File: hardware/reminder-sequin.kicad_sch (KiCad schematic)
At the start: 10 parts, among them SW1 User, SW2 RST, U1 STM32G041J6Mx

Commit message: power system
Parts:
- added BT1: Battery_Cell, Battery:BatteryHolder_Keystone_2466_1xAAA, symbol Device:Battery_Cell
- added C3, C4, C5: 10uF, Capacitor_SMD:C_0805_2012Metric, symbol Device:C
- added D2: SS24, Diode_SMD:D_SMA, symbol Device:D_Schottky
- added F1: Polyfuse, Fuse:Fuse_1206_3216Metric, symbol Device:Polyfuse
- added JP1: ISENSE, Jumper:SolderJumper-2_P1.3mm_Bridged2Bar_RoundedPad1.0x1.5mm, symbol Jumper:Jumper_2_Open
- added JP2: SolderJumper_2_Bridged, Jumper:SolderJumper-2_P1.3mm_Bridged2Bar_RoundedPad1.0x1.5mm, symbol Jumper:SolderJumper_2_Bridged
- added JP3: Power_Bypass, Jumper:SolderJumper-2_P1.3mm_Bridged2Bar_RoundedPad1.0x1.5mm, symbol Jumper:SolderJumper_2_Bridged
- added L1: 2.7uH, cat:Inductor_0806, symbol Device:L
- added R5: 487k, symbol Device:R
- added R6: 100k, symbol Device:R
- added U2: ~, symbol cat:TPS61023DRL
- D1, R1, R3: now not fitted
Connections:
- net GND: now also BT1.2 (-), C3.2, C4.2, C5.2, D2.2 (A), R6.2, U2.4 (GND)
- net VDD: now also JP3.2 (B)
- new net: C3.1, D2.1 (K), F1.2, JP2.1 (A), L1.1, U2.2 (EN), U2.3 (VIN)
- new net: C4.1, C5.1, JP3.1 (A), R5.1, U2.6 (VOUT)
- new net: R5.2, R6.1, U2.1 (FB)
- new net: L1.2, U2.5 (SW)
- new net: F1.1, JP1.2 (B)
- new net: BT1.1 (+), JP1.1 (A)
- new net BATTERY_SENSE: JP2.2 (B)

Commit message: stuff
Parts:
- removed U1: STM32G041J6Mx, Package_SO:SOIC-8_3.9x4.9mm_P1.27mm, symbol MCU_ST_STM32G0:STM32G041J6Mx
- added R7: 100k, symbol Device:R
- added U1: STM32G031F6Px, Package_SO:TSSOP-20_4.4x6.5mm_P0.65mm, symbol MCU_ST_STM32G0:STM32G031F6Px
- added U3: STM32G031J6Mx, Package_SO:SOIC-8_3.9x4.9mm_P1.27mm, symbol MCU_ST_STM32G0:STM32G031J6Mx
- D1: Cost (none) -> .5
- U2: value ~ -> TPS61023DRL; footprint (none) -> Package_TO_SOT_SMD:SOT-563; LCSC Part # (none) -> C919459
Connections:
- net BATTERY_SENSE: now also R7.1, U3.6 (PA10/PA12); no longer JP2.2 (B)
- net BUTTON: now also U3.8 (PA14/PA15/PB5/PB6)
- net GND: now also U1.5 (VSS), U3.3 (VSS)
- net LED: now also U3.1 (PB7/PB8/PB9/PC14)
- net NRST: now also U3.4 (PA0/PA1/PA2/PF2)
- net PHOTORESISTOR: now also U3.5 (PA8/PA9/PA11/PB0/PB1)
- net SWCK: now also U3.7 (PA13)
- net VDD: now also U1.4 (VDD), U3.2 (VDD)
- new net: JP2.2 (B), R7.2

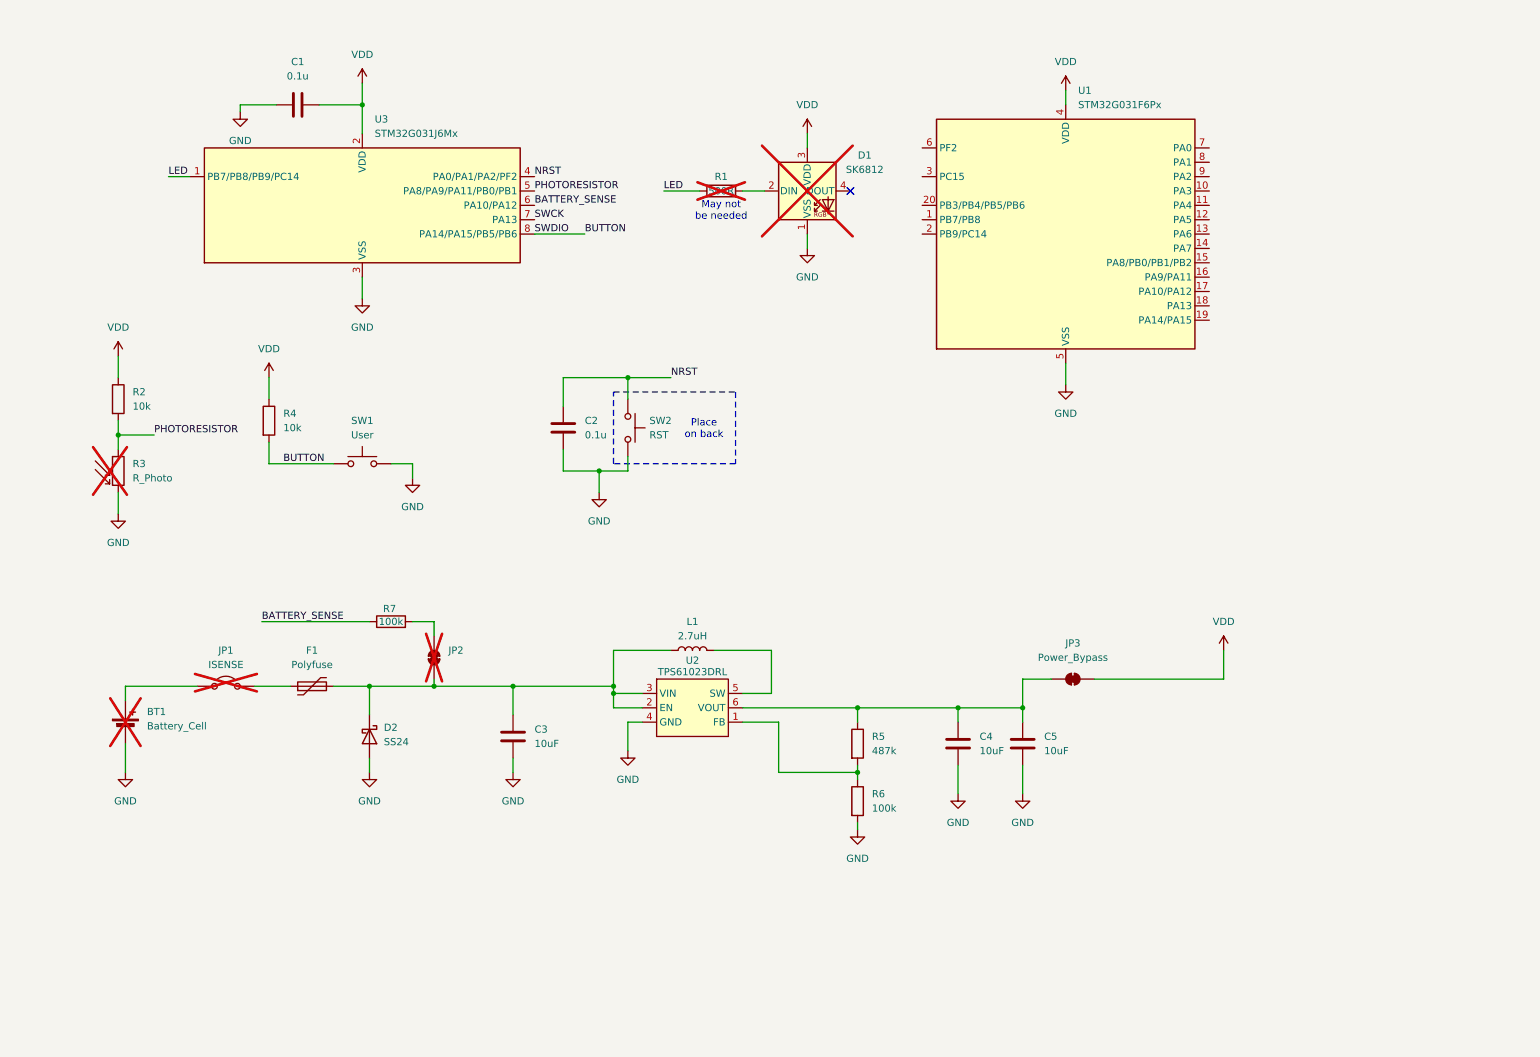
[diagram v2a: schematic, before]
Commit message: switched to rp2040
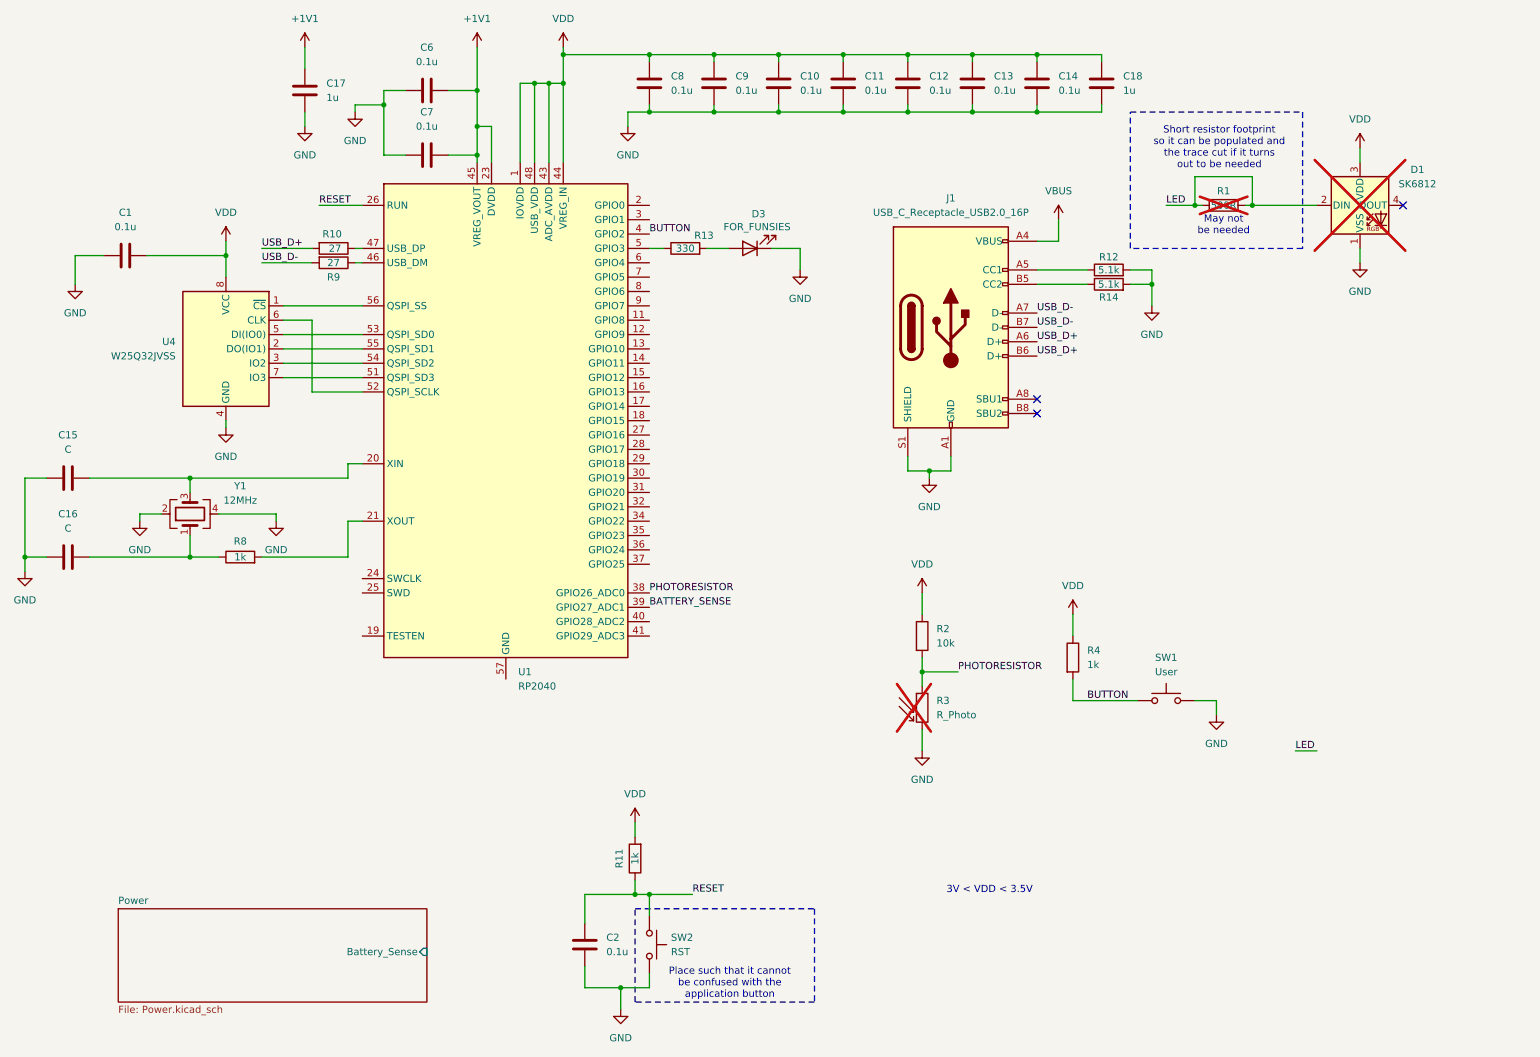
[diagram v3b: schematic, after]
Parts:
- removed BT1: Battery_Cell, Battery:BatteryHolder_Keystone_2466_1xAAA, symbol Device:Battery_Cell
- removed C3, C4, C5: 10uF, Capacitor_SMD:C_0805_2012Metric, symbol Device:C
- removed D2: SS24, Diode_SMD:D_SMA, symbol Device:D_Schottky
- removed F1: Polyfuse, Fuse:Fuse_1206_3216Metric, symbol Device:Polyfuse
- removed JP1: ISENSE, Jumper:SolderJumper-2_P1.3mm_Bridged2Bar_RoundedPad1.0x1.5mm, symbol Jumper:Jumper_2_Open
- removed JP2: SolderJumper_2_Bridged, Jumper:SolderJumper-2_P1.3mm_Bridged2Bar_RoundedPad1.0x1.5mm, symbol Jumper:SolderJumper_2_Bridged
- removed JP3: Power_Bypass, Jumper:SolderJumper-2_P1.3mm_Bridged2Bar_RoundedPad1.0x1.5mm, symbol Jumper:SolderJumper_2_Bridged
- removed L1: 2.7uH, cat:Inductor_0806, symbol Device:L
- removed R5: 487k, symbol Device:R
- removed R6, R7: 100k, symbol Device:R
- removed U1: STM32G031F6Px, Package_SO:TSSOP-20_4.4x6.5mm_P0.65mm, symbol MCU_ST_STM32G0:STM32G031F6Px
- removed U2: TPS61023DRL, Package_TO_SOT_SMD:SOT-563, symbol cat:TPS61023DRL
- removed U3: STM32G031J6Mx, Package_SO:SOIC-8_3.9x4.9mm_P1.27mm, symbol MCU_ST_STM32G0:STM32G031J6Mx
- added C10, C11, C12, C13, C14, C6, C7, C8, C9: 0.1u, Capacitor_SMD:C_0603_1608Metric, symbol Device:C
- added C15, C16: C, symbol Device:C
- added C17, C18: 1u, Capacitor_SMD:C_0805_2012Metric, symbol Device:C
- added D3: FOR_FUNSIES, symbol Device:LED
- added J1: USB_C_Receptacle_USB2.0_16P, Connector_USB:USB_C_Receptacle_G-Switch_GT-USB-7010ASV, symbol Connector:USB_C_Receptacle_USB2.0_16P
- added R10, R9: 27, Resistor_SMD:R_0603_1608Metric, symbol Device:R
- added R11, R8: 1k, Resistor_SMD:R_0603_1608Metric, symbol Device:R
- added R12, R14: 5.1k, Resistor_SMD:R_0603_1608Metric, symbol Device:R
- added R13: 330, Resistor_SMD:R_0603_1608Metric, symbol Device:R
- added U1: RP2040, Package_DFN_QFN:QFN-56-1EP_7x7mm_P0.4mm_EP3.2x3.2mm, symbol MCU_RaspberryPi:RP2040
- added U4: W25Q32JVSS, Package_SO:SOIC-8_5.23x5.23mm_P1.27mm, symbol Memory_Flash:W25Q32JVSS
- added Y1: 12MHz, symbol Device:Crystal_GND24
- C1, C2: footprint (none) -> Capacitor_SMD:C_0603_1608Metric; LCSC Part # (none) -> C14663
- R1: footprint (none) -> Resistor_SMD:R_0603_1608Metric
- R2: footprint (none) -> Resistor_SMD:R_0603_1608Metric; LCSC Part # (none) -> C25804
- R3: footprint (none) -> Connector_JST:JST_XH_B2B-XH-AM_1x02_P2.50mm_Vertical
- R4: value 10k -> 1k; footprint (none) -> Resistor_SMD:R_0603_1608Metric; LCSC Part # (none) -> C21190
- SW1, SW2: footprint (none) -> Button_Switch_SMD:SW_Push_1P1T_XKB_TS-1187A; LCSC Part # (none) -> C318884
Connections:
- net BATTERY_SENSE: now also U1.39 (GPIO27_ADC1)
- net BUTTON: now also U1.4 (GPIO2)
- net GND: now also C10.1, C11.1, C12.1, C13.1, C14.1, C15.1, C16.1, C17.1, C18.1, C6.1, C7.1, C8.1, C9.1, D3.1 (K), J1.A1 (GND), J1.A12 (GND), J1.B1 (GND), J1.B12 (GND), J1.S1 (SHIELD), R12.2, R14.2, U4.4 (GND), Y1.2, Y1.4
- net LED: now also D1.2 (DIN), R1.2
- net PHOTORESISTOR: now also U1.38 (GPIO26_ADC0)
- net VDD: now also C10.2, C11.2, C12.2, C13.2, C14.2, C18.2, C8.2, C9.2, R11.2, U1.1 (IOVDD), U1.10 (IOVDD), U1.22 (IOVDD), U1.33 (IOVDD), U1.42 (IOVDD), U1.43 (ADC_AVDD), U1.44 (VREG_IN), U1.48 (USB_VDD), U1.49 (IOVDD), U4.8 (VCC)
- net NRST renamed RESET
- net RESET: now also R11.1, U1.26 (RUN)
- new net: C15.2, U1.20 (XIN), Y1.3
- new net: C16.2, R8.1, Y1.1
- new net: R8.2, U1.21 (XOUT)
- new net: R13.1, U1.5 (GPIO3)
- new net: D3.2 (A), R13.2
- new net: J1.B5 (CC2), R14.1
- new net: U1.56 (QSPI_SS), U4.1 (~{CS})
- new net: U1.55 (QSPI_SD1), U4.2 (DO(IO1))
- new net: U1.54 (QSPI_SD2), U4.3 (IO2)
- new net: U1.53 (QSPI_SD0), U4.5 (DI(IO0))
- new net: U1.52 (QSPI_SCLK), U4.6 (CLK)
- new net: U1.51 (QSPI_SD3), U4.7 (IO3)
- new net: R9.1, U1.46 (USB_DM)
- new net: R10.1, U1.47 (USB_DP)
- new net: J1.A5 (CC1), R12.1
- new net +1V1: C17.2, C6.2, C7.2, U1.23 (DVDD), U1.45 (VREG_VOUT), U1.50 (DVDD)
- new net USB_D+: J1.A6 (D+), J1.B6 (D+), R10.2
- new net USB_D-: J1.A7 (D-), J1.B7 (D-), R9.2
- new net VBUS: J1.A4 (VBUS), J1.A9 (VBUS), J1.B4 (VBUS), J1.B9 (VBUS)
- no-connect marks 1 -> 3
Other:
- added sheet Power (Power.kicad_sch)
- note added: "3V < VDD < 3.5V"
- note added: "Place such that it cannot be confused with the application button"
- note added: "Short resistor footprint so it can be populated and the trace cut if it turns out to be needed"
- note removed: "Place on back"
- moved on the sheet: C2, D1, R1, R2, R3, R4, SW1, SW2

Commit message: almost done
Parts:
- added C19: 0.1u, Capacitor_SMD:C_0603_1608Metric, symbol Device:C
- added R15, R16, R17, R19, R20: 5.1k, Resistor_SMD:R_0603_1608Metric, symbol Device:R
- added R18, R22: 10k, Resistor_SMD:R_0603_1608Metric, symbol Device:R
- added R21: 1k, Resistor_SMD:R_0603_1608Metric, symbol Device:R
- added SW3: BOOTSEL, symbol Switch:SW_Push
- added TP1, TP2: TestPoint, symbol Connector:TestPoint
- added U3: FM24C64B, Package_SO:SOIC-8_3.9x4.9mm_P1.27mm, symbol Memory_NVRAM:FM24C64B
- SW1, SW2: footprint Button_Switch_SMD:SW_Push_1P1T_XKB_TS-1187A -> (none); LCSC Part # C318884 -> C720477
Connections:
- net BUTTON: now also U1.9 (GPIO7); no longer U1.4 (GPIO2)
- net GND: now also U1.19 (TESTEN), U1.57 (GND), C19.2, R15.1, R16.1, R17.1, SW3.2, U3.4 (VSS)
- net VDD: now also C19.1, R18.1, R19.2, R20.2, R22.1, U3.8 (VDD)
- net at R13.1: now also U1.11 (GPIO8); no longer U1.5 (GPIO3)
- net QSPI_CS: now reaches U1.56 (QSPI_SS), U4.1 (~{CS})
- net QSPI_CS: now also R21.1
- net at U1.2 (GPIO0): now also TP1.1
- net at U1.3 (GPIO1): now also TP2.1
- net EEPROM_WP: now reaches U1.6 (GPIO4)
- net EEPROM_WP: now also R18.2, U3.7 (WP)
- new net: R17.2, U3.1 (A0)
- new net: R16.2, U3.2 (A1)
- new net: R15.2, U3.3 (A2)
- new net: R21.2, R22.2, SW3.1
- new net SCL: R19.1, U1.5 (GPIO3), U3.5 (SDA)
- new net SDA: R20.1, U1.4 (GPIO2), U3.6 (SCL)
- no-connect marks 3 -> 5
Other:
- moved on the sheet: D3, R13

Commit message: more stuff
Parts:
- C1, C10, C11, C12, C13, C14, C19, C2, C6, C7, C8, C9: value 0.1u -> 0.1uF
- C15, C16: value C -> 15pF; footprint (none) -> Capacitor_SMD:C_0603_1608Metric; LCSC Part # (none) -> C1644
- C17, C18: value 1u -> 1uF
- D3, Y1: footprint (none) -> Crystal:Crystal_SMD_Abracon_ABM8G-4Pin_3.2x2.5mm
- SW1, SW2: footprint (none) -> TestPoint:TestPoint_Pad_3.0x3.0mm
- TP1, TP2: footprint (none) -> TestPoint:TestPoint_Pad_3.0x3.0mm; now not fitted
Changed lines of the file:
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@@
 			)
 		)
-		(property "Value" "C"
+		(property "Value" "15pF"
 			(at 24.13 90.17 90)
 			(effects
@@
 			)
 		)
-		(property "Footprint" ""
+		(property "Footprint" "Capacitor_SMD:C_0603_1608Metric"
 			(at 27.94 94.2848 0)
 			(effects
@@
 			)
 		)
+		(property "LCSC Part #" "C1644 "
+			(at 24.13 95.25 0)
+			(effects
+				(font
+					(size 1.27 1.27)
+				)
+				(hide yes)
+			)
+		)
 		(pin "2"
 		)
@@
 			)
 		)
-		(property "Value" "0.1u"
+		(property "Value" "0.1uF"
 			(at 87.63 21.59 90)
 			(effects
@@
 			)
 		)
-		(property "Footprint" ""
+		(property "Footprint" "TestPoint:TestPoint_Pad_3.0x3.0mm"
 			(at 132.08 177.8 0)
 			(effects
@@
 			)
 		)
-		(property "Value" "0.1u"
+		(property "Value" "0.1uF"
 			(at 187.96 26.6699 0)
 			(effects
@@
 			)
 		)
-		(property "Value" "0.1u"
+		(property "Value" "0.1uF"
 			(at 153.67 26.6699 0)
 			(effects
@@
 			)
 		)
-		(property "Value" "0.1u"
+		(property "Value" "0.1uF"
 			(at 176.53 26.6699 0)
 			(effects
@@
 			)
 		)
-		(property "Value" "0.1u"
+		(property "Value" "0.1uF"
 			(at 119.38 179.0699 0)
 			(effects
@@
 			)
 		)
-		(property "Value" "0.1u"
+		(property "Value" "0.1uF"
 			(at 142.24 26.6699 0)
 			(effects
@@
 			)
 		)
-		(property "Value" "0.1u"
+		(property "Value" "0.1uF"
 			(at 130.81 26.6699 0)
 			(effects
@@
 			)
 		)
-		(property "Value" "0.1u"
+		(property "Value" "0.1uF"
 			(at 87.63 33.02 90)
 			(effects
@@
 			)
 		)
-		(property "Value" "0.1u"
+		(property "Value" "0.1uF"
 			(at 165.1 26.6699 0)
 			(effects
@@
 			)
 		)
-		(property "Value" "1u"
+		(property "Value" "1uF"
 			(at 210.82 26.6699 0)
 			(effects
@@
 		(in_bom yes)
 		(on_board yes)
-		(dnp no)
+		(dnp yes)
 		(fields_autoplaced yes)
 		(property "Reference" "TP1"
@@
 			)
 		)
-		(property "Footprint" ""
+		(property "Footprint" "TestPoint:TestPoint_Pad_3.0x3.0mm"
 			(at 137.16 44.45 0)
 			(effects
@@
 			)
 		)
-		(property "Value" "1u"
+		(property "Value" "1uF"
 			(at 69.85 27.9399 0)
 			(effects
@@
 			)
 		)
-		(property "Value" "0.1u"
+		(property "Value" "0.1uF"
 			(at 34.29 50.8 90)
 			(effects
@@
 			)
 		)
-		(property "Value" "C"
+		(property "Value" "15pF"
 			(at 24.13 104.14 90)
 			(effects
@@
 			)
 		)
-		(property "Footprint" ""
+		(property "Footprint" "Capacitor_SMD:C_0603_1608Metric"
 			(at 27.94 108.2548 0)
 			(effects
@@
 			)
 		)
+		(property "LCSC Part #" "C1644 "
+			(at 24.13 109.22 0)
+			(effects
+				(font
+					(size 1.27 1.27)
+				)
+				(hide yes)
+			)
+		)
 		(pin "2"
 		)
@@
 			)
 		)
-		(property "Footprint" ""
+		(property "Footprint" "Crystal:Crystal_SMD_Abracon_ABM8G-4Pin_3.2x2.5mm"
 			(at 144.78 67.31 0)
 			(effects
@@
 			)
 		)
-		(property "Value" "0.1u"
+		(property "Value" "0.1uF"
 			(at 240.03 69.85 90)
 			(effects
@@
 			)
 		)
-		(property "Footprint" ""
+		(property "Footprint" "TestPoint:TestPoint_Pad_3.0x3.0mm"
 			(at 218.44 129.54 0)
 			(effects
@@
 			)
 		)
-		(property "Footprint" ""
+		(property "Footprint" "Crystal:Crystal_SMD_Abracon_ABM8G-4Pin_3.2x2.5mm"
 			(at 45.72 101.6 0)
 			(effects
@@
 		(in_bom yes)
 		(on_board yes)
-		(dnp no)
+		(dnp yes)
 		(fields_autoplaced yes)
 		(property "Reference" "TP2"
@@
 			)
 		)
-		(property "Footprint" ""
+		(property "Footprint" "TestPoint:TestPoint_Pad_3.0x3.0mm"
 			(at 149.86 44.45 0)
 			(effects
@@
 			)
 		)
-		(property "Value" "0.1u"
+		(property "Value" "0.1uF"
 			(at 199.39 26.6699 0)
 			(effects

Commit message: assigned part numbers and footprints
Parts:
- D3: footprint Crystal:Crystal_SMD_Abracon_ABM8G-4Pin_3.2x2.5mm -> (none)
- R18, R2, R22: LCSC Part # C25804 -> C25804
- SW1, SW2: footprint TestPoint:TestPoint_Pad_3.0x3.0mm -> cat:TS-1088-AR02016
- SW3: footprint (none) -> cat:TS-1088-AR02016
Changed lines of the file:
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@@
 			)
 		)
-		(property "LCSC Part #" "     C25804"
+		(property "LCSC Part #" " C25804"
 			(at 175.26 123.19 0)
 			(effects
@@
 			)
 		)
-		(property "Footprint" "TestPoint:TestPoint_Pad_3.0x3.0mm"
+		(property "Footprint" "cat:TS-1088-AR02016"
 			(at 132.08 177.8 0)
 			(effects
@@
 			)
 		)
-		(property "LCSC Part #" "     C25804"
+		(property "LCSC Part #" " C25804"
 			(at 57.15 125.73 0)
 			(effects
@@
 			)
 		)
-		(property "Footprint" ""
+		(property "Footprint" "cat:TS-1088-AR02016"
 			(at 62.23 140.97 0)
 			(effects
@@
 			)
 		)
-		(property "Footprint" "Crystal:Crystal_SMD_Abracon_ABM8G-4Pin_3.2x2.5mm"
+		(property "Footprint" ""
 			(at 144.78 67.31 0)
 			(effects
@@
 			)
 		)
-		(property "Footprint" "TestPoint:TestPoint_Pad_3.0x3.0mm"
+		(property "Footprint" "cat:TS-1088-AR02016"
 			(at 218.44 129.54 0)
 			(effects
@@
 			)
 		)
-		(property "LCSC Part #" "     C25804"
+		(property "LCSC Part #" " C25804"
 			(at 275.59 83.82 0)
 			(effects

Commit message: stuff
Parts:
- D3: footprint (none) -> LED_SMD:LED_0805_2012Metric; LCSC Part # (none) -> C2296
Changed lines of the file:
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@@
 			)
 		)
-		(property "Footprint" ""
+		(property "Footprint" "LED_SMD:LED_0805_2012Metric"
 			(at 144.78 67.31 0)
 			(effects
@@
 			(at 144.78 67.31 0)
 			(effects
+				(font
+					(size 1.27 1.27)
+				)
+				(hide yes)
+			)
+		)
+		(property "LCSC Part #" "C2296"
+			(at 144.78 67.31 0)
+			(effects
